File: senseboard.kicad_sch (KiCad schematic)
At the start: 83 parts, among them J1 USB_C_Receptacle_USB2.0_16P, J2 Screw_Terminal_01x02, J3 DM3AT-SF-PEJM5, J4 Conn_01x04, J5 Conn_01x08, U1 USBLC6-2SC6, U10 EMIF06-MSD02N16, U11 BME690, U2 TPS62840DLCR, U3 TPS62840DLCR, U4 SCD41-D-R2, U5 SGP41-D-R4, U6 SGP41-D-R4, U7 SHT4x, U8 STM32L4Q5CGUx, U9 RFM95W-915S2, Y1 Crystal_GND3

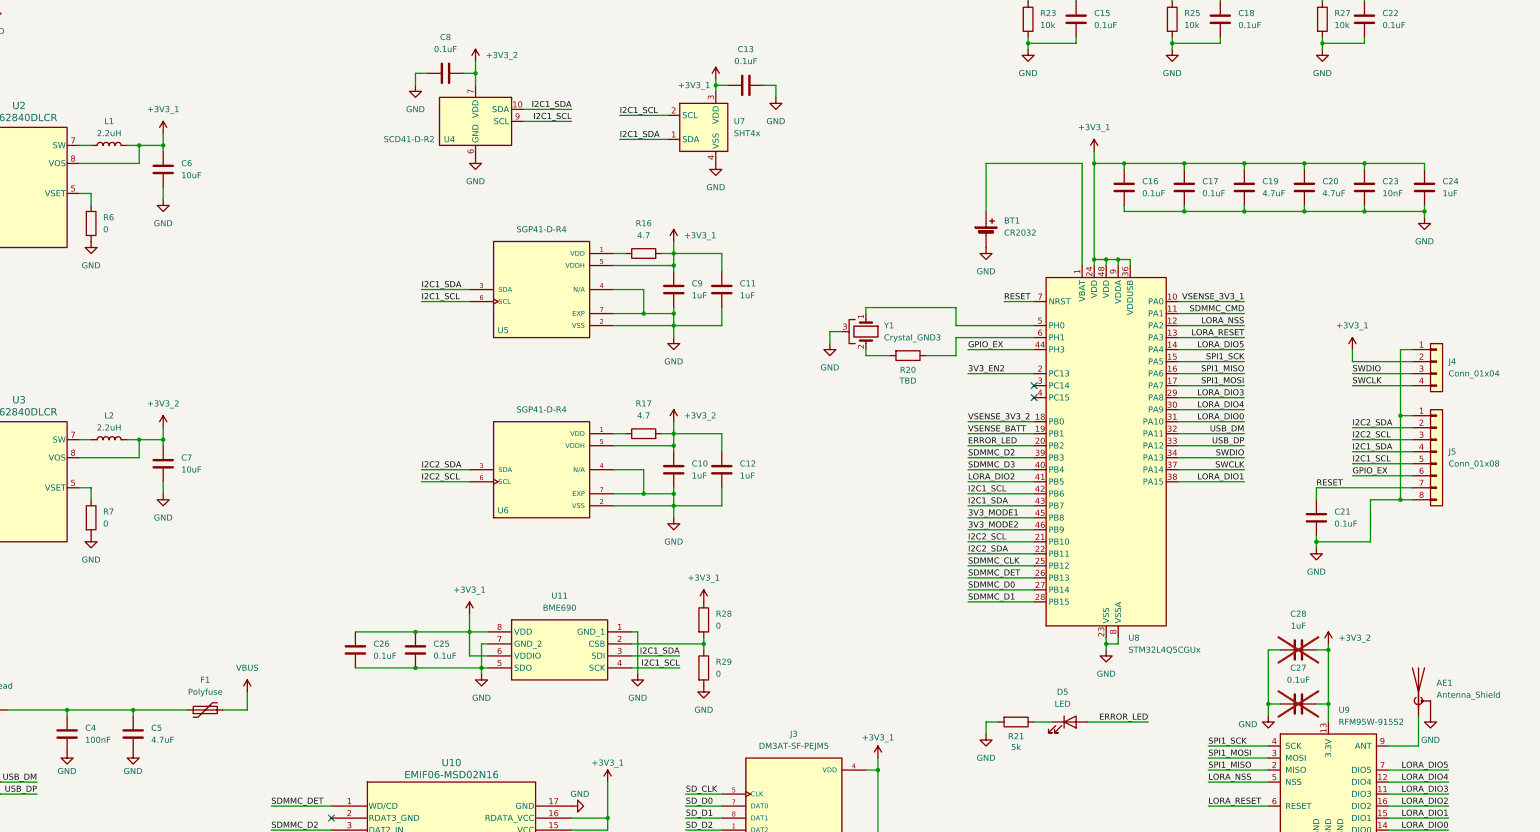
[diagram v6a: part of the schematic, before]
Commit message: added blocking protection for coin cell and charge limiting
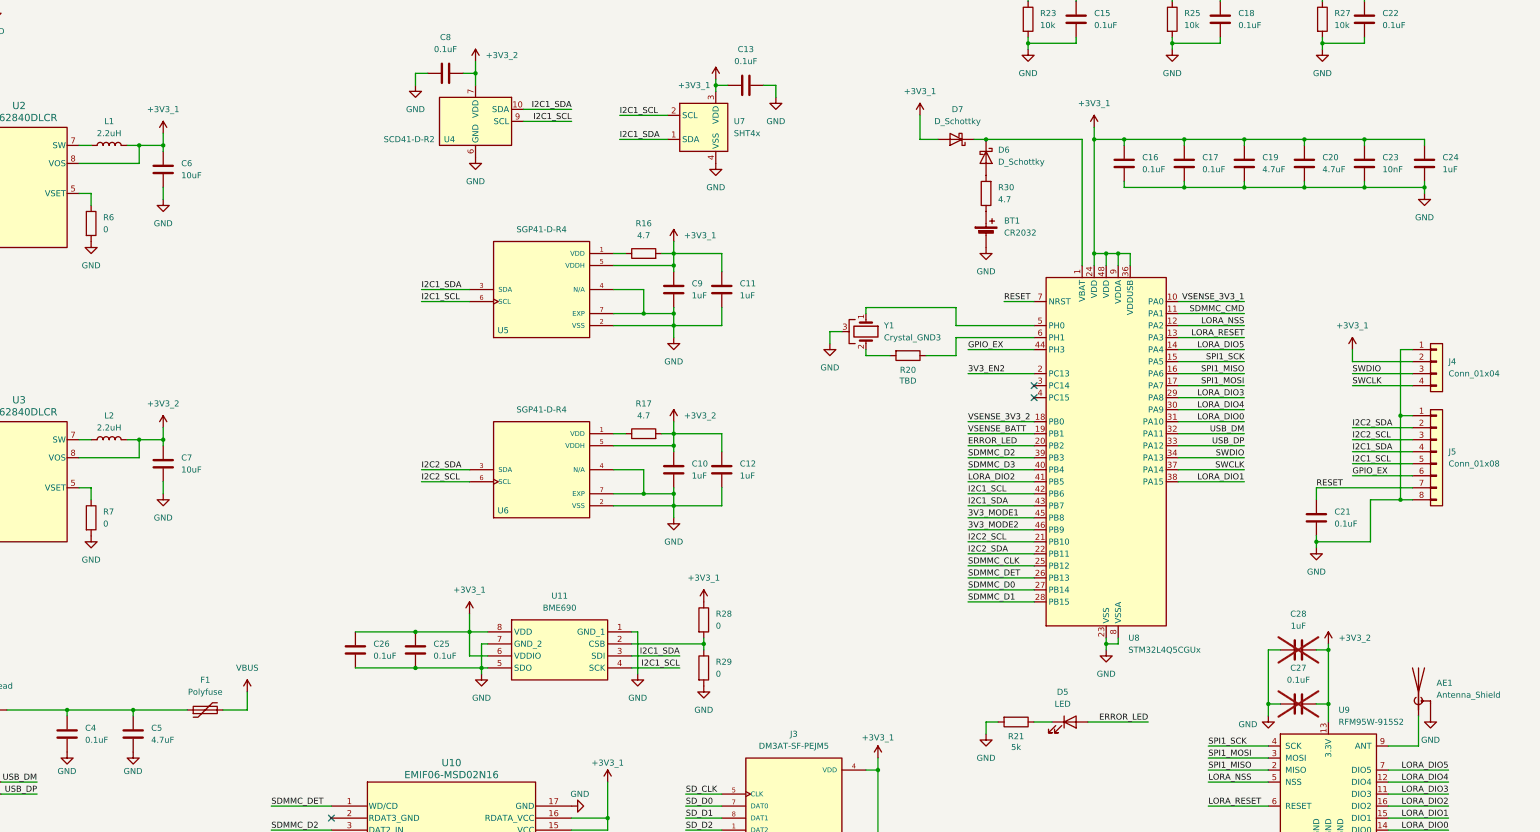
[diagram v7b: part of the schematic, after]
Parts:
- added D6, D7: D_Schottky, Diode_SMD:D_SOD-523, symbol Device:D_Schottky
- added R30: 4.7, Resistor_SMD:R_0603_1608Metric, symbol Device:R
- C4: value 100nF -> 0.1uF
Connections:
- net +3V3_1: now also D7.2 (A)
- net at U8.1 (VBAT): now also D6.1 (K), D7.1 (K); no longer BT1.1 (+)
- new net: D6.2 (A), R30.2
- new net: BT1.1 (+), R30.1
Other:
- moved on the sheet: C16, C17, C19, C20, C23, C24

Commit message: added lots of additional resistors and caps for added decoupling and modification if neccesary, finalized layout and added graphics
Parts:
- removed U2, U3: TPS62840DLCR, TPS62840DLCR:VSON8_2P1X1P6_TEX, symbol TPS62840DLCR:TPS62840DLCR
- added C29, C30, C31, C32: 33pF, Capacitor_SMD:C_0402_1005Metric, symbol Device:C
- added C33: 0.1uF, Capacitor_SMD:C_0402_1005Metric, symbol Device:C
- added C34: 10uF, Capacitor_SMD:C_0805_2012Metric, symbol Device:C
- added R10, R12, R13, R14, R31, R32, R33, R8: 0, Resistor_SMD:R_0402_1005Metric, symbol Device:R
- added U2, U3: TPS62849DLCR, TPS62849DLCR:VSON8_2P1X1P6_TEX, symbol TPS62849DLCR:TPS62849DLCR
- added Y2: Crystal, Crystal:Crystal_SMD_EuroQuartz_EQ161-2Pin_3.2x1.5mm, symbol Device:Crystal
- D6, D7: value D_Schottky -> BAT54WX-TP
- R20: value TBD -> 0
- R30: value 4.7 -> 330
- Y1: symbol Device:Crystal_GND3 -> Device:Crystal_GND2
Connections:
- net +3V3_1: now also C34.1, R32.1, U2.8 (VOS)
- net +3V3_2: now also U3.8 (VOS)
- net 3V3_EN1: now also U2.4 (EN)
- net 3V3_EN2: now also U3.4 (EN)
- net 3V3_MODE1: now also R12.1, U2.3 (MODE)
- net 3V3_MODE2: now also R13.1, U3.3 (MODE)
- net GND: now also Y1.2, C29.2, C30.1, C31.2, C32.2, C33.1, C34.2, R10.2, R12.2, R13.2, R14.2, R33.2, R8.2, U2.1 (GND), U3.1 (GND); no longer U11.5 (SDO), Y1.3
- net at C1.1, D1.1 (K), D2.1 (K)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: now also U2.2 (VIN)
- net at L1.1: now also U2.7 (SW)
- net at Y1.1: now also R20.2, C29.1; no longer U8.5 (PH0)
- net at R6.1: now also U2.5 (VSET)
- net at C2.1, D3.1 (K), D4.1 (K): now also U3.2 (VIN)
- net OSC32_IN: now reaches U8.3 (PC14)
- net OSC32_IN: now also C31.1, Y2.1
- net OSC32_OUT: now reaches U8.4 (PC15)
- net OSC32_OUT: now also C32.1, Y2.2
- net at BT1.1 (+), R30.1: now also C33.2
- net at R7.1: now also U3.5 (VSET)
- net at L2.1: now also U3.7 (SW)
- net GPIO_EX renamed GPIO_EX/BOOT0
- net GPIO_EX/BOOT0: now also R14.1
- new net: C30.2, R31.1, Y1.3
- new net: R31.2, U8.5 (PH0)
- new net 3V3_STOP1: R8.1, U2.6 (STOP)
- new net 3V3_STOP2: R10.1, U3.6 (STOP)
- new net SDO: R32.2, R33.1, U11.5 (SDO)
- no-connect marks 7 -> 3
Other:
- moved on the sheet: C25, C26, J4, R20, Y1
